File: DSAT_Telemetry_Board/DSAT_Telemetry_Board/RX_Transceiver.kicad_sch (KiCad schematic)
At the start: 4 parts

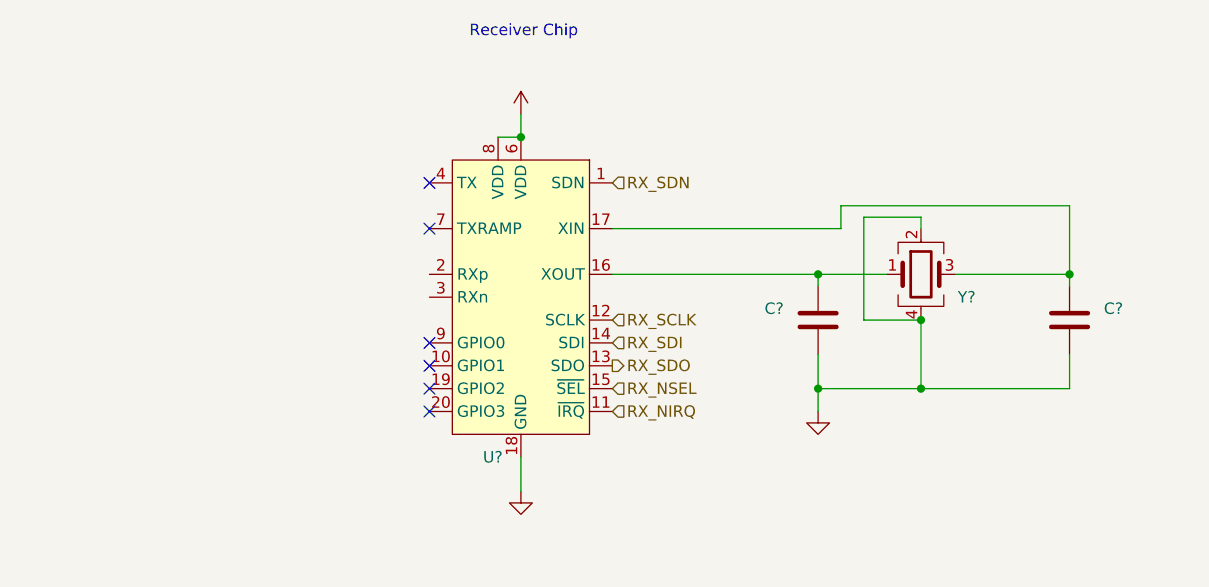
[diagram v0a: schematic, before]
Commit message: antenna matching netowrks for Rx and Tx added partially
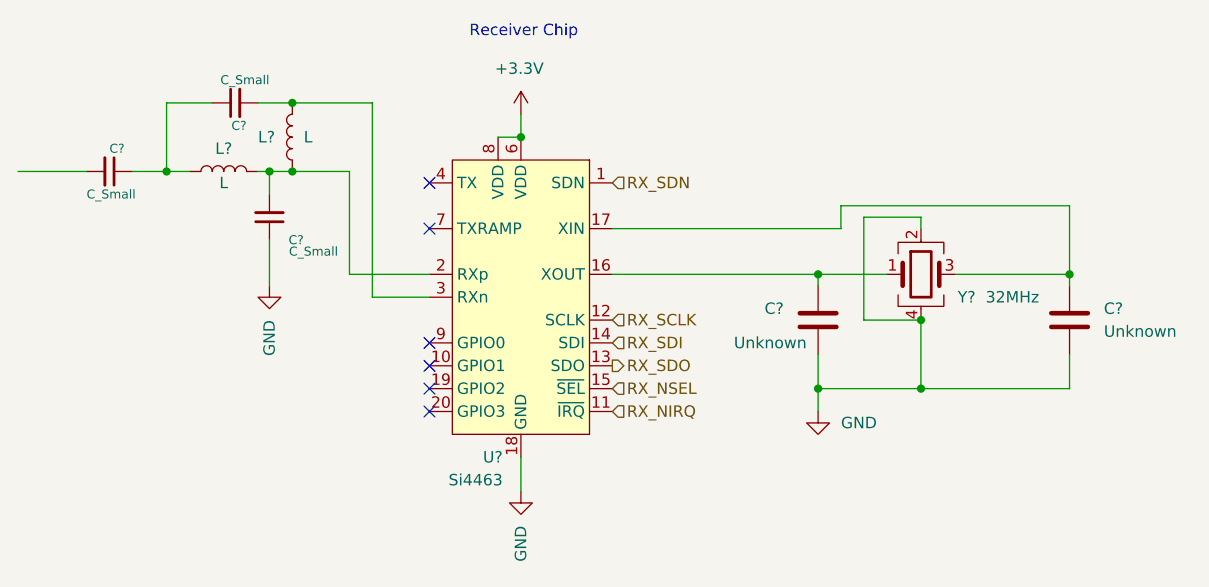
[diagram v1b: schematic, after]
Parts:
- added C? (x3): C_Small, symbol Device:C_Small
- added L? (x2): L, symbol Device:L
- C? (x2): value (none) -> Unknown
- U?: value (none) -> Si4463; footprint (none) -> Package_DFN_QFN:QFN-20-1EP_4x4mm_P0.5mm_EP2.6x2.6mm_ThermalVias
- Y?: value (none) -> 32MHz
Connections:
- net GND: now also C?.1
- net at U?.2 (RXp): now also C?.2, L?.1, L?.2
- net at U?.3 (RXn): now also C?.2, L?.2
- new net: C?.1, C?.1, L?.1
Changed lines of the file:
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@@
   (junction (at 187.96 85.09) (diameter 0) (color 0 0 0 0)
   )
+  (junction (at 87.63 73.66) (diameter 0) (color 0 0 0 0)
+  )
+  (junction (at 99.06 73.66) (diameter 0) (color 0 0 0 0)
+  )
+  (junction (at 101.6 66.04) (diameter 0) (color 0 0 0 0)
+  )
   (junction (at 127 69.85) (diameter 0) (color 0 0 0 0)
+  )
+  (junction (at 101.6 73.66) (diameter 0) (color 0 0 0 0)
   )
   (junction (at 171.45 97.79) (diameter 0) (color 0 0 0 0)
@@
     (stroke (width 0) (type default) (color 0 0 0 0))
   )
+  (wire (pts (xy 101.6 66.04) (xy 110.49 66.04))
+    (stroke (width 0) (type default) (color 0 0 0 0))
+  )
   (wire (pts (xy 187.96 93.98) (xy 187.96 97.79))
     (stroke (width 0) (type default) (color 0 0 0 0))
   )
+  (wire (pts (xy 71.12 73.66) (xy 78.74 73.66))
+    (stroke (width 0) (type default) (color 0 0 0 0))
+  )
   (wire (pts (xy 187.96 86.36) (xy 187.96 85.09))
     (stroke (width 0) (type default) (color 0 0 0 0))
   )
+  (wire (pts (xy 83.82 73.66) (xy 87.63 73.66))
+    (stroke (width 0) (type default) (color 0 0 0 0))
+  )
   (wire (pts (xy 160.02 93.98) (xy 160.02 97.79))
     (stroke (width 0) (type default) (color 0 0 0 0))
   )
+  (wire (pts (xy 90.17 73.66) (xy 87.63 73.66))
+    (stroke (width 0) (type default) (color 0 0 0 0))
+  )
+  (wire (pts (xy 107.95 73.66) (xy 107.95 85.09))
+    (stroke (width 0) (type default) (color 0 0 0 0))
+  )
   (wire (pts (xy 127 67.31) (xy 127 69.85))
     (stroke (width 0) (type default) (color 0 0 0 0))
   )
+  (wire (pts (xy 99.06 76.2) (xy 99.06 73.66))
+    (stroke (width 0) (type default) (color 0 0 0 0))
+  )
+  (wire (pts (xy 99.06 86.36) (xy 99.06 81.28))
+    (stroke (width 0) (type default) (color 0 0 0 0))
+  )
   (wire (pts (xy 127 105.41) (xy 127 109.22))
     (stroke (width 0) (type default) (color 0 0 0 0))
@@
     (stroke (width 0) (type default) (color 0 0 0 0))
   )
+  (wire (pts (xy 110.49 87.63) (xy 116.84 87.63))
+    (stroke (width 0) (type default) (color 0 0 0 0))
+  )
   (wire (pts (xy 137.16 85.09) (xy 160.02 85.09))
     (stroke (width 0) (type default) (color 0 0 0 0))
@@
     (stroke (width 0) (type default) (color 0 0 0 0))
   )
+  (wire (pts (xy 99.06 73.66) (xy 101.6 73.66))
+    (stroke (width 0) (type default) (color 0 0 0 0))
+  )
   (wire (pts (xy 165.1 78.74) (xy 165.1 90.17))
     (stroke (width 0) (type default) (color 0 0 0 0))
   )
+  (wire (pts (xy 87.63 66.04) (xy 92.71 66.04))
+    (stroke (width 0) (type default) (color 0 0 0 0))
+  )
   (wire (pts (xy 162.56 77.47) (xy 162.56 80.01))
     (stroke (width 0) (type default) (color 0 0 0 0))
@@
     (stroke (width 0) (type default) (color 0 0 0 0))
   )
+  (wire (pts (xy 101.6 73.66) (xy 107.95 73.66))
+    (stroke (width 0) (type default) (color 0 0 0 0))
+  )
   (wire (pts (xy 137.16 80.01) (xy 162.56 80.01))
     (stroke (width 0) (type default) (color 0 0 0 0))
   )
+  (wire (pts (xy 97.79 73.66) (xy 99.06 73.66))
+    (stroke (width 0) (type default) (color 0 0 0 0))
+  )
   (wire (pts (xy 187.96 85.09) (xy 187.96 77.47))
     (stroke (width 0) (type default) (color 0 0 0 0))
   )
+  (wire (pts (xy 107.95 85.09) (xy 116.84 85.09))
+    (stroke (width 0) (type default) (color 0 0 0 0))
+  )
+  (wire (pts (xy 87.63 73.66) (xy 87.63 66.04))
+    (stroke (width 0) (type default) (color 0 0 0 0))
+  )
+  (wire (pts (xy 110.49 66.04) (xy 110.49 87.63))
+    (stroke (width 0) (type default) (color 0 0 0 0))
+  )
   (wire (pts (xy 160.02 85.09) (xy 160.02 86.36))
+    (stroke (width 0) (type default) (color 0 0 0 0))
+  )
+  (wire (pts (xy 97.79 66.04) (xy 101.6 66.04))
     (stroke (width 0) (type default) (color 0 0 0 0))
   )
@@
       (effects (font (size 1.27 1.27)) (justify right))
     )
-    (property "Value" "" (id 1) (at 158.75 92.71 0)
+    (property "Value" "Unknown" (id 1) (at 158.75 92.71 0)
       (effects (font (size 1.27 1.27)) (justify right))
     )
@@
     )
     (property "Datasheet" "~" (id 3) (at 160.02 90.17 0)
+      (effects (font (size 1.27 1.27)) hide)
+    )
+    (pin "1")
+    (pin "2")
+  )
+  (symbol (lib_id "Device:L") (at 101.6 69.85 180) (unit 1)
+    (in_bom yes) (on_board yes)
+    (property "Reference" "L?" (id 0) (at 97.79 69.85 0)
+      (effects (font (size 1.27 1.27)) (justify right))
+    )
+    (property "Value" "L" (id 1) (at 102.87 69.85 0)
+      (effects (font (size 1.27 1.27)) (justify right))
+    )
+    (property "Footprint" "" (id 2) (at 101.6 69.85 0)
+      (effects (font (size 1.27 1.27)) hide)
+    )
+    (property "Datasheet" "~" (id 3) (at 101.6 69.85 0)
       (effects (font (size 1.27 1.27)) hide)
     )
@@
       (effects (font (size 1.27 1.27)) (justify left))
     )
-    (property "Value" "" (id 1) (at 191.77 91.4399 0)
+    (property "Value" "Unknown" (id 1) (at 191.77 91.4399 0)
       (effects (font (size 1.27 1.27)) (justify left))
     )
@@
       (effects (font (size 1.27 1.27)) hide)
     )
-    (property "Value" "" (id 1) (at 162.56 101.5999 0)
+    (property "Value" "GND" (id 1) (at 162.56 101.5999 0)
       (effects (font (size 1.27 1.27)) (justify left))
     )
@@
     (pin "1")
   )
+  (symbol (lib_id "Device:C_Small") (at 95.25 66.04 90) (unit 1)
+    (in_bom yes) (on_board yes)
+    (property "Reference" "C?" (id 0) (at 96.52 68.58 90)
+      (effects (font (size 1 1)) (justify left))
+    )
+    (property "Value" "C_Small" (id 1) (at 99.06 63.5 90)
+      (effects (font (size 1 1)) (justify left))
+    )
+    (property "Footprint" "" (id 2) (at 95.25 66.04 0)
+      (effects (font (size 1.27 1.27)) hide)
+    )
+    (property "Datasheet" "~" (id 3) (at 95.25 66.04 0)
+      (effects (font (size 1.27 1.27)) hide)
+    )
+    (pin "1")
+    (pin "2")
+  )
+  (symbol (lib_id "Device:C_Small") (at 81.28 73.66 270) (unit 1)
+    (in_bom yes) (on_board yes)
+    (property "Reference" "C?" (id 0) (at 81.28 71.12 90)
+      (effects (font (size 1 1)) (justify left))
+    )
+    (property "Value" "C_Small" (id 1) (at 78.74 76.2 90)
+      (effects (font (size 1 1)) (justify left))
+    )
+    (property "Footprint" "" (id 2) (at 81.28 73.66 0)
+      (effects (font (size 1.27 1.27)) hide)
+    )
+    (property "Datasheet" "~" (id 3) (at 81.28 73.66 0)
+      (effects (font (size 1.27 1.27)) hide)
+    )
+    (pin "1")
+    (pin "2")
+  )
   (symbol (lib_id "power:+3.3V") (at 127 67.31 0) (unit 1)
     (in_bom yes) (on_board yes)
@@
       (effects (font (size 1.27 1.27)) hide)
     )
-    (property "Value" "" (id 1) (at 129.54 62.23 0)
+    (property "Value" "+3.3V" (id 1) (at 129.54 62.23 0)
       (effects (font (size 1.27 1.27)) (justify right))
     )
@@
     )
     (pin "1")
+  )
+  (symbol (lib_id "Device:L") (at 93.98 73.66 90) (unit 1)
+    (in_bom yes) (on_board yes)
+    (property "Reference" "L?" (id 0) (at 93.98 71.12 90))
+    (property "Value" "L" (id 1) (at 93.98 74.93 90))
+    (property "Footprint" "" (id 2) (at 93.98 73.66 0)
+      (effects (font (size 1.27 1.27)) hide)
+    )
+    (property "Datasheet" "~" (id 3) (at 93.98 73.66 0)
+      (effects (font (size 1.27 1.27)) hide)
+    )
+    (pin "1")
+    (pin "2")
   )
   (symbol (lib_id "power:GND") (at 127 109.22 0) (mirror y) (unit 1)
@@
       (effects (font (size 1.27 1.27)) hide)
     )
-    (property "Value" "" (id 1) (at 127.0001 113.03 90)
+    (property "Value" "GND" (id 1) (at 127.0001 113.03 90)
       (effects (font (size 1.27 1.27)) (justify right))
     )
@@
     (in_bom yes) (on_board yes)
     (property "Reference" "Y?" (id 0) (at 176.53 87.63 0))
-    (property "Value" "" (id 1) (at 181.61 87.63 0))
+    (property "Value" "32MHz" (id 1) (at 181.61 87.63 0))
     (property "Footprint" "" (id 2) (at 171.45 85.09 0)
       (effects (font (size 1.27 1.27)) hide)
@@
     (pin "3")
     (pin "4")
+  )
+  (symbol (lib_id "power:GND") (at 99.06 86.36 0) (mirror y) (unit 1)
+    (in_bom yes) (on_board yes) (fields_autoplaced)
+    (property "Reference" "#PWR?" (id 0) (at 99.06 92.71 0)
+      (effects (font (size 1.27 1.27)) hide)
+    )
+    (property "Value" "GND" (id 1) (at 99.0601 90.17 90)
+      (effects (font (size 1.27 1.27)) (justify right))
+    )
+    (property "Footprint" "" (id 2) (at 99.06 86.36 0)
+      (effects (font (size 1.27 1.27)) hide)
+    )
+    (property "Datasheet" "" (id 3) (at 99.06 86.36 0)
+      (effects (font (size 1.27 1.27)) hide)
+    )
+    (pin "1")
+  )
+  (symbol (lib_id "Device:C_Small") (at 99.06 78.74 180) (unit 1)
+    (in_bom yes) (on_board yes)
+    (property "Reference" "C?" (id 0) (at 102.87 81.28 0)
+      (effects (font (size 1 1)) (justify left))
+    )
+    (property "Value" "C_Small" (id 1) (at 106.68 82.55 0)
+      (effects (font (size 1 1)) (justify left))
+    )
+    (property "Footprint" "" (id 2) (at 99.06 78.74 0)
+      (effects (font (size 1.27 1.27)) hide)
+    )
+    (property "Datasheet" "~" (id 3) (at 99.06 78.74 0)
+      (effects (font (size 1.27 1.27)) hide)
+    )
+    (pin "1")
+    (pin "2")
   )
   (symbol (lib_id "RF:Si4463") (at 127 87.63 0) (mirror y) (unit 1)
@@
       (effects (font (size 1.27 1.27)) (justify left))
     )
-    (property "Value" "" (id 1) (at 124.9806 107.95 0)
-      (effects (font (size 1.27 1.27)) (justify left))
-    )
-    (property "Footprint" "" (id 2) (at 127 57.15 0)
-      (effects (font (size 1.27 1.27)) hide)
-    )
+    (property "Value" "Si4463" (id 1) (at 124.9806 107.95 0)
+      (effects (font (size 1.27 1.27)) (justify left))
+    )
+    (property "Footprint" "Package_DFN_QFN:QFN-20-1EP_4x4mm_P0.5mm_EP2.6x2.6mm_ThermalVias" (id 2) (at 127 57.15 0)
+      (effects (font (size 1.27 1.27)) hide)
+    )

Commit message: More footprints
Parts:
- C? (x5): footprint (none) -> Capacitor_SMD:C_0201_0603Metric
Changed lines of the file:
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@@
       (effects (font (size 1.27 1.27)) (justify right))
     )
-    (property "Footprint" "" (id 2) (at 160.9852 86.36 0)
+    (property "Footprint" "Capacitor_SMD:C_0201_0603Metric" (id 2) (at 160.9852 86.36 0)
       (effects (font (size 1.27 1.27)) hide)
     )
@@
       (effects (font (size 1.27 1.27)) (justify left))
     )
-    (property "Footprint" "" (id 2) (at 188.9252 93.98 0)
+    (property "Footprint" "Capacitor_SMD:C_0201_0603Metric" (id 2) (at 188.9252 93.98 0)
       (effects (font (size 1.27 1.27)) hide)
     )
@@
       (effects (font (size 1 1)) (justify left))
     )
-    (property "Footprint" "" (id 2) (at 95.25 66.04 0)
+    (property "Footprint" "Capacitor_SMD:C_0201_0603Metric" (id 2) (at 95.25 66.04 0)
       (effects (font (size 1.27 1.27)) hide)
     )
@@
       (effects (font (size 1 1)) (justify left))
     )
-    (property "Footprint" "" (id 2) (at 81.28 73.66 0)
+    (property "Footprint" "Capacitor_SMD:C_0201_0603Metric" (id 2) (at 81.28 73.66 0)
       (effects (font (size 1.27 1.27)) hide)
     )
@@
       (effects (font (size 1 1)) (justify left))
     )
-    (property "Footprint" "" (id 2) (at 99.06 78.74 0)
+    (property "Footprint" "Capacitor_SMD:C_0201_0603Metric" (id 2) (at 99.06 78.74 0)
       (effects (font (size 1.27 1.27)) hide)
     )
